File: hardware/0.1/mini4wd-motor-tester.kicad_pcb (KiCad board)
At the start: 2 copper layers, 93 parts, among them J1 USB_C_Receptacle_USB2.0_16P, J2 JST SH, J3 JST SH, M1 Motor_DC, SW1 RA, SW2 RA, SW3 EC11, U1 TLV62130, U2 USBLC6-2SC6, U3 RT9080-33GJ5, U4 MCP4725, U5 ESP32-S3-WROOM-1, U6 INA219AxDCN, U7 DRV8837, U8 GP2S700HCP, U9 TMP1075DSG

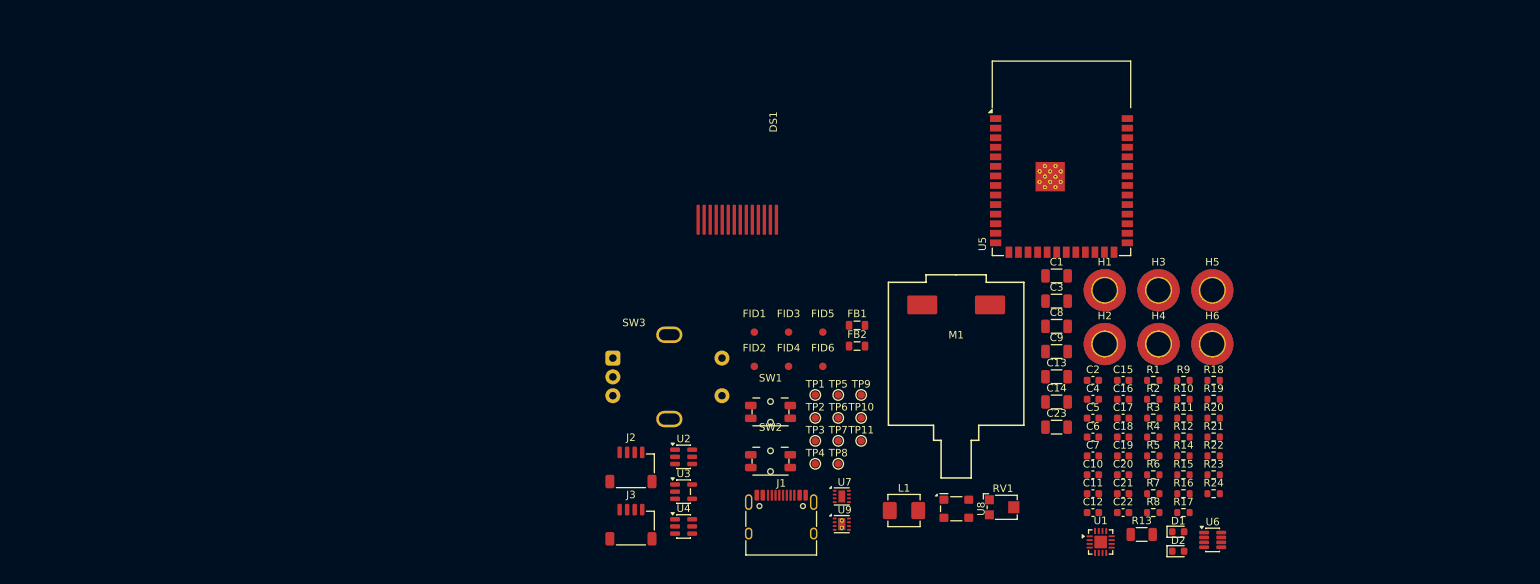
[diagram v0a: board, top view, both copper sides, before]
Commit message: rough component placement
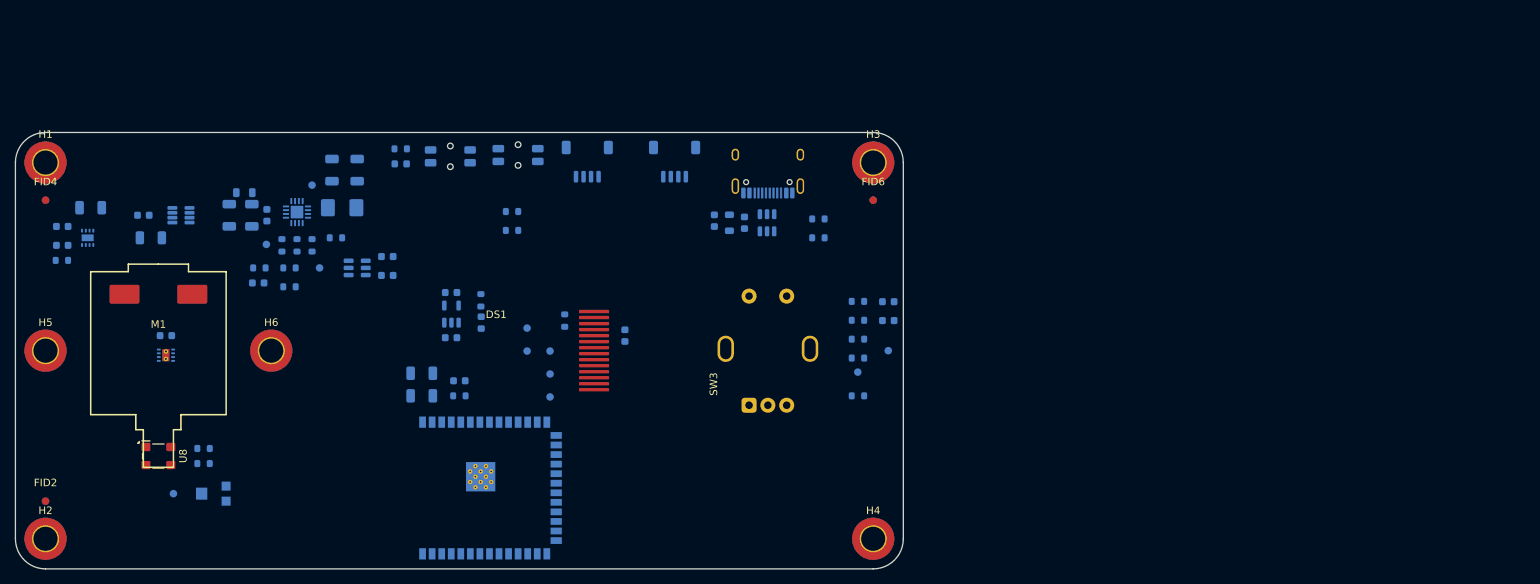
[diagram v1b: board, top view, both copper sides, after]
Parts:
- C1, C10, C11, C12, C13, C14, C15, C16, C17, C18, C19, C2, C20, C21, C22, C23, C3, C4, C5, C6, C7, C8, C9, D1, D2, FB1, FB2, FID1, FID3, FID5, J1, J2, J3, L1, R1, R10, R11, R12, R13, R14, R15, R16, R17, R18, R19, R2, R20, R21, R22, R23, R24, R3, R4, R5, R6, R7, R8, R9, RV1, SW1, SW2, TP1, TP10, TP11, TP2, TP3, TP4, TP5, TP6, TP7, TP8, TP9, U1, U2, U3, U4, U5, U6, U7, U9: moved to B.Cu
- moved H5 155.3 mm to (70.0, 100.0)
- moved R11 150.5 mm to (72.2, 88.0), turned to 180 degrees
- moved U6 143.7 mm to (88.0, 82.0), turned to 180 degrees
- moved C17 143.3 mm to (72.2, 83.5)
- moved H2 143.1 mm to (70.0, 125.0)
- moved C16 142.5 mm to (72.2, 86.0)
- moved H1 141.8 mm to (70.0, 75.0)
- moved R13 137.5 mm to (84.0, 85.0), turned to 180 degrees
- moved R22 134.2 mm to (91.0, 113.0), turned to 180 degrees
- moved C15 132.0 mm to (83.0, 82.0), turned to 180 degrees
- moved C23 131.6 mm to (76.0, 81.0)
- moved R17 130.4 mm to (91.0, 115.0), turned to 180 degrees
- moved C22 129.4 mm to (86.0, 98.0), turned to 180 degrees
- moved H6 125.1 mm to (100.0, 100.0)
- moved R9 121.1 mm to (101.4, 86.0), turned to -90 degrees
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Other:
- board outline added: 118 x 58 mm

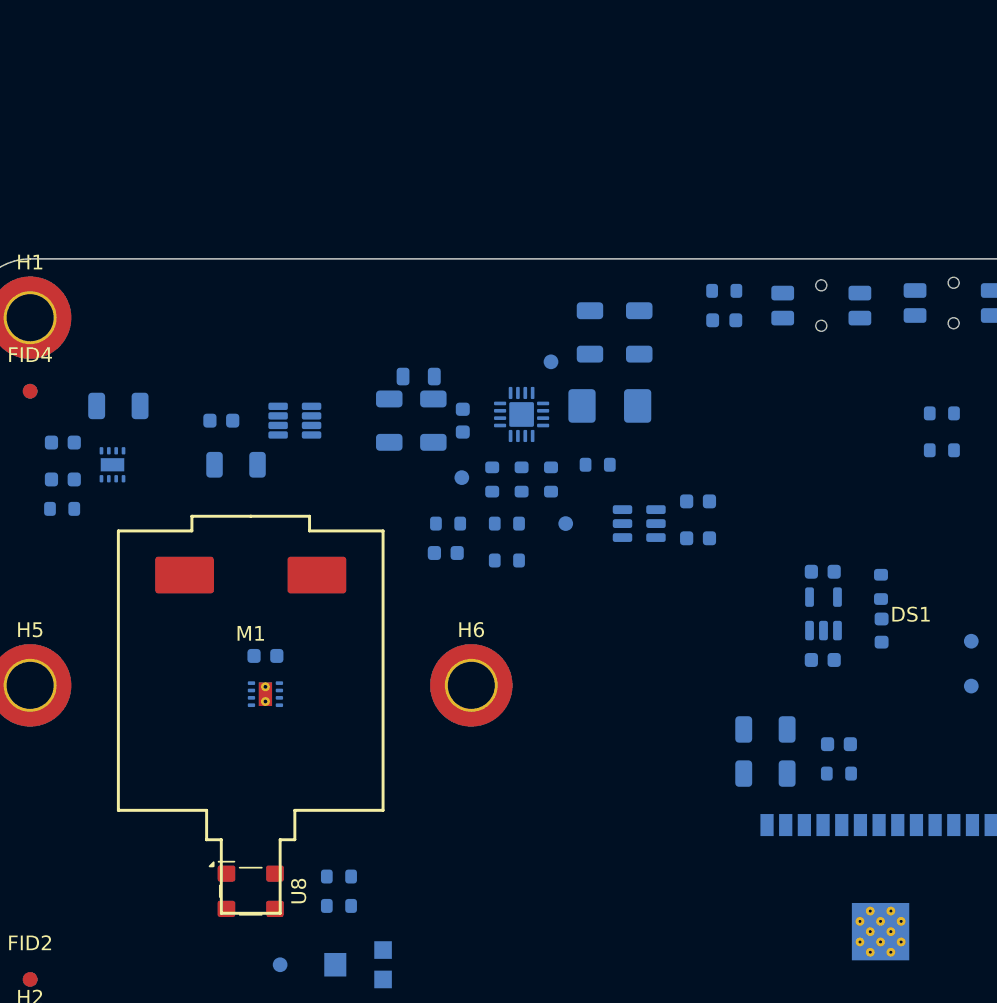
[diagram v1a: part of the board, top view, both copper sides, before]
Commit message: add wheel rpm, aux 5V circuits
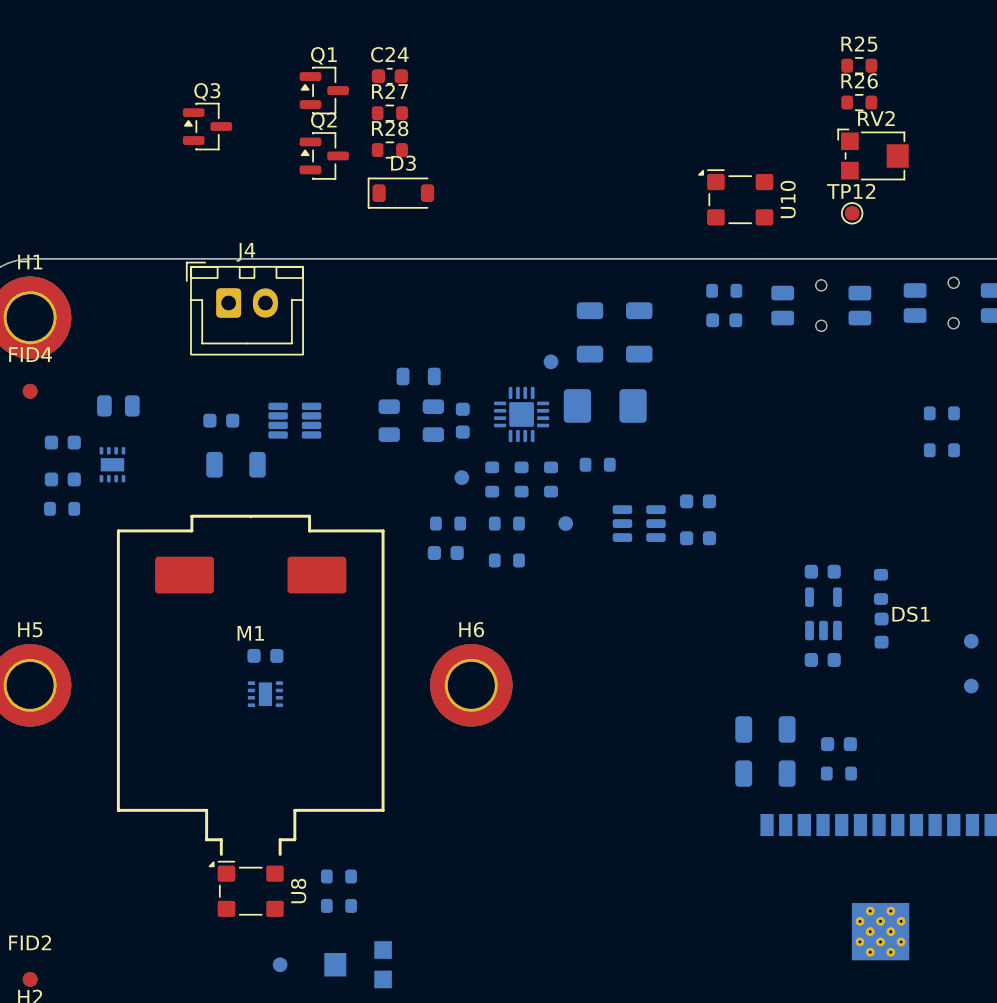
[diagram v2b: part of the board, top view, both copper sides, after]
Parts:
- added C24: 100n, Capacitor_SMD:C_0603_1608Metric, F.Cu at (94.5, 58.6)
- added D3: B5819W, Diode_SMD:D_SOD-123, F.Cu at (95.4, 66.5)
- added J4: JST XH, Connector_JST:JST_XH_B2B-XH-A_1x02_P2.50mm_Vertical, F.Cu at (83.5, 74.0)
- added Q1: 2N7002, Package_TO_SOT_SMD:SOT-23, F.Cu at (90.0, 59.5)
- added Q2: AO3401A, Package_TO_SOT_SMD:SOT-23, F.Cu at (90.0, 64.0)
- added Q3: 2N7002, Package_TO_SOT_SMD:SOT-23, F.Cu at (82.1, 62.0)
- added R25: 22R, Resistor_SMD:R_0603_1608Metric, F.Cu at (126.4, 57.9)
- added R26: 2K2, Resistor_SMD:R_0603_1608Metric, F.Cu at (126.4, 60.4)
- added R27: 10K, Resistor_SMD:R_0603_1608Metric, F.Cu at (94.5, 61.1)
- added R28: 10K, Resistor_SMD:R_0603_1608Metric, F.Cu at (94.5, 63.6)
- added RV2: POT_10K, josh-passives-smt:Potentiometer_Bourns_TC33X_Vertical, F.Cu at (127.5, 64.0)
- added TP12: TP, TestPoint:TestPoint_Pad_D1.0mm, F.Cu at (125.9, 67.9)
- added U10: GP2S700HCP, josh-passives-smt:Sharp_GP2S700HCP, F.Cu at (118.3, 67.0)
- C1, C23, C3: footprint Capacitor_SMD:C_1206_3216Metric -> Capacitor_SMD:C_0805_2012Metric
- U9: footprint Package_SON:WSON-8-1EP_2x2mm_P0.5mm_EP0.9x1.6mm_ThermalVias -> Package_SON:WSON-8-1EP_2x2mm_P0.5mm_EP0.9x1.6mm
- moved L1 0.31 mm to (109.1, 81.0)
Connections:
- net /RPM_OUT renamed /MOTOR_OUT
- U5 pad 38: unconnected-(U5-IO2-Pad38) -> /AUX_5V_EN
- U5 pad 39: unconnected-(U5-IO1-Pad39) -> /WHEEL_OUT

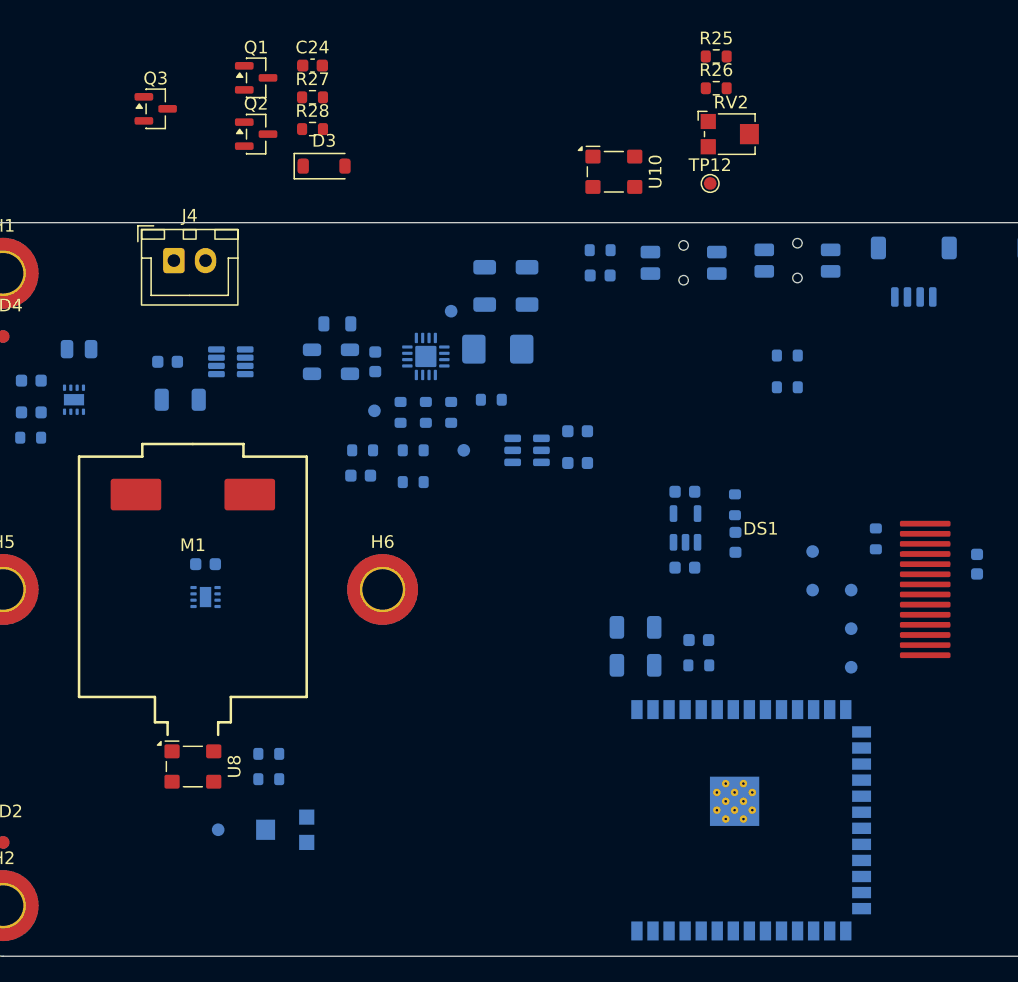
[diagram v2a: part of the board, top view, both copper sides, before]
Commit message: update motor cutout, provision space for wheel speed tester
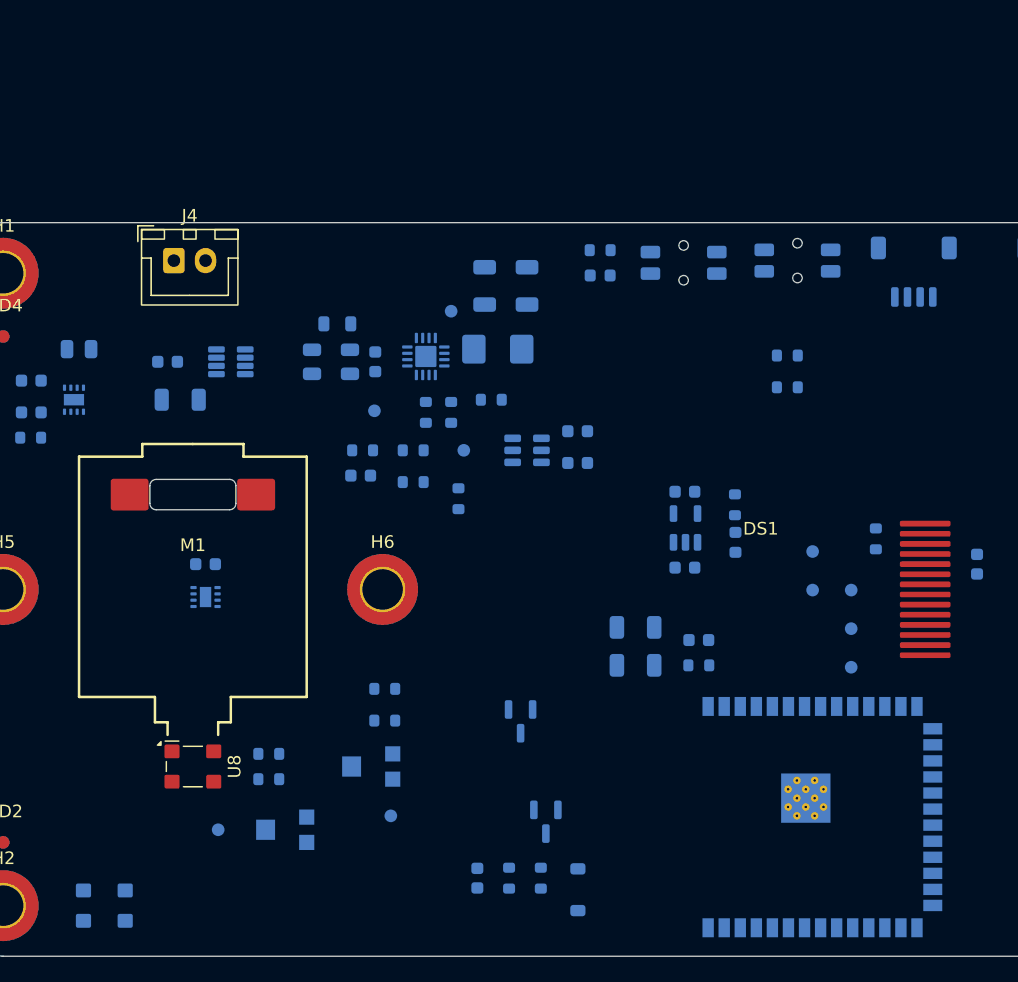
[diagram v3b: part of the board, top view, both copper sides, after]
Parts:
- removed Q1: 2N7002, Package_TO_SOT_SMD:SOT-23
- C24, D3, Q2, Q3, R25, R26, R27, R28, RV2, TP12, U10: moved to B.Cu
- R8: value 22K -> 30K
- R9: value 75K -> 100K
- moved U10 70.6 mm to (78.0, 125.0), turned to 180 degrees
- moved C24 65.6 mm to (107.5, 122.8), turned to -90 degrees
- moved R27 63.7 mm to (110.0, 122.8), turned to -90 degrees
- moved R28 61.9 mm to (112.5, 122.8), turned to -90 degrees
- moved D3 60.6 mm to (115.4, 123.7), turned to -90 degrees
- moved Q2 59.0 mm to (112.9, 118.4), turned to -90 degrees
- moved RV2 57.6 mm to (99.0, 114.0), turned to 180 degrees
- moved R25 56.5 mm to (100.2, 107.9), turned to 180 degrees
- moved R26 56.5 mm to (100.2, 110.4), turned to 180 degrees
- moved Q3 56.4 mm to (110.9, 110.4), turned to -90 degrees
- moved TP12 56.0 mm to (100.7, 117.9), turned to 180 degrees
- moved R9 8.22 mm to (106.0, 92.8), turned to 90 degrees
- moved U5 5.64 mm to (131.0, 118.0)

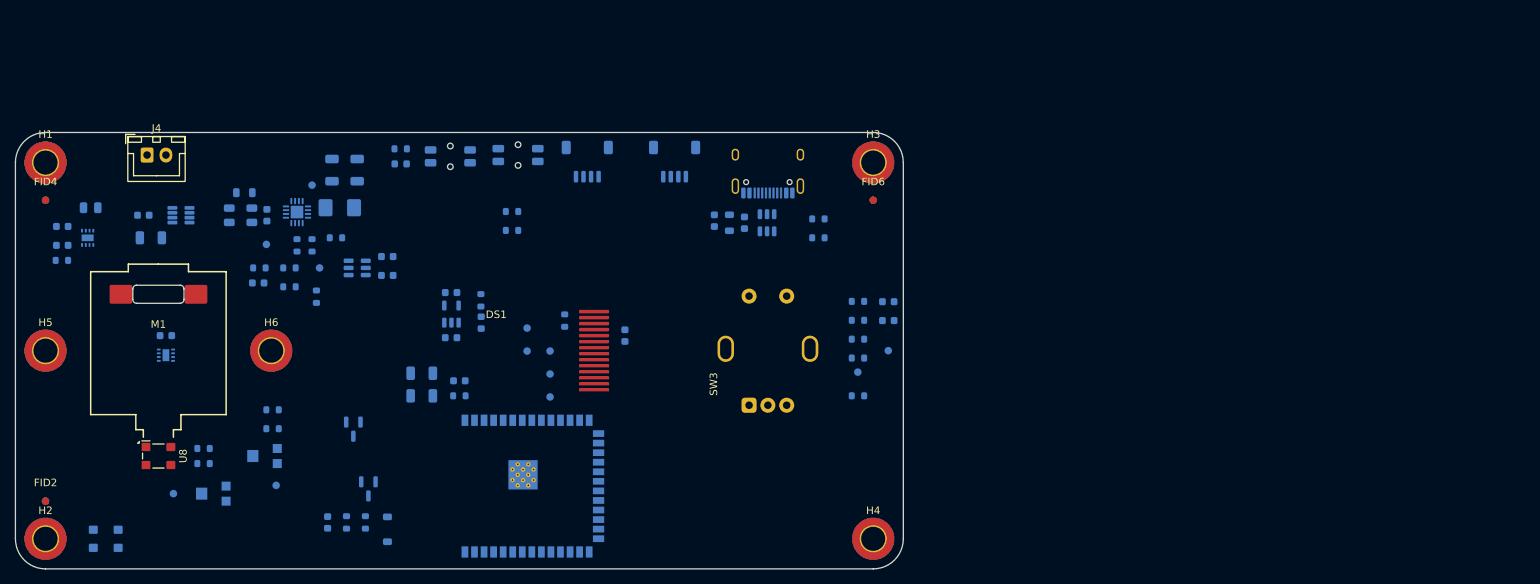
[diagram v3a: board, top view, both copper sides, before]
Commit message: shrinking board down
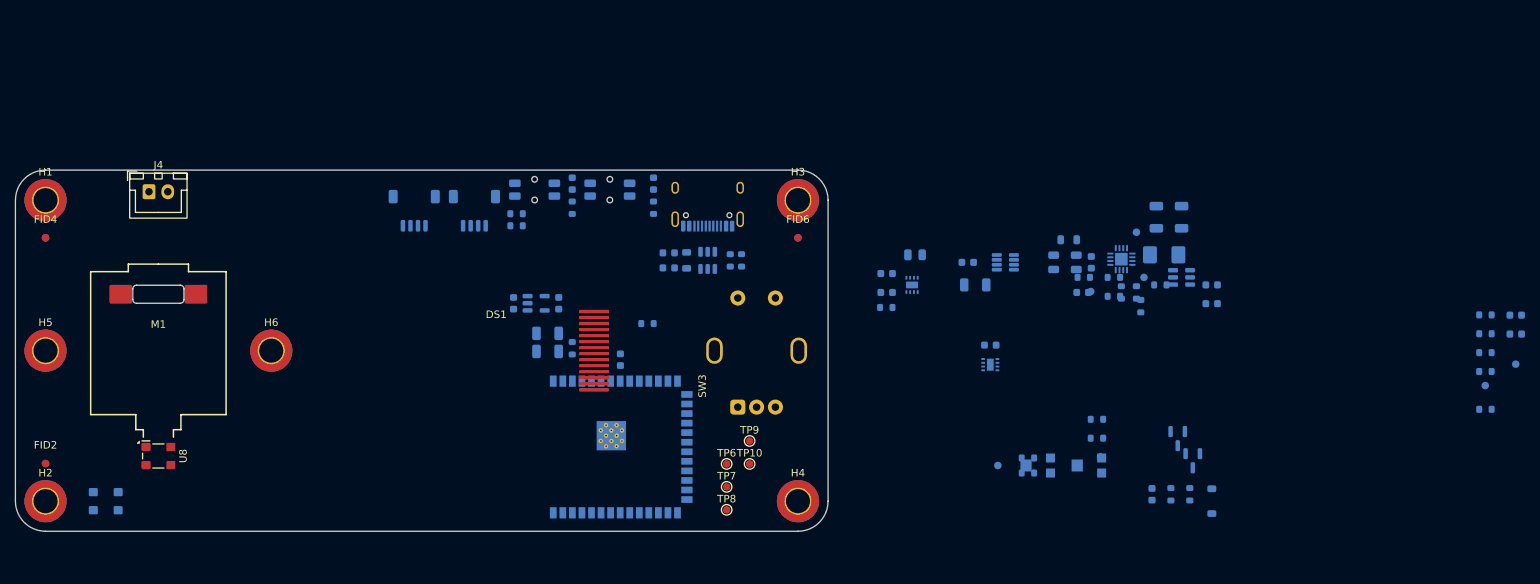
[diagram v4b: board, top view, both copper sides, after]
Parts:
- removed C18: 1u, Capacitor_SMD:C_0603_1608Metric
- TP10, TP6, TP7, TP8, TP9: moved to F.Cu
- moved L1 109.7 mm to (218.7, 87.3)
- moved R11 109.7 mm to (181.7, 94.3)
- moved C15 109.7 mm to (192.6, 88.3)
- moved C16 109.7 mm to (181.8, 92.3)
- moved C17 109.7 mm to (181.8, 89.8)
- moved C23 109.7 mm to (185.6, 87.3)
- moved C9 109.7 mm to (217.6, 82.3)
- moved R13 109.7 mm to (193.6, 91.3)
- moved R6 109.7 mm to (218.2, 91.3)
- moved U6 109.7 mm to (197.6, 88.3)
- moved U7 109.7 mm to (185.2, 91.3)
- moved C1 109.7 mm to (204.0, 88.3)
- moved C12 109.7 mm to (225.0, 93.8)
- moved C3 109.7 mm to (207.0, 88.3)
- moved C4 109.7 mm to (209.0, 88.3)
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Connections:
- net Net-(J2-Pin_3) renamed /TXD
- net Net-(J2-Pin_4) renamed /RXD
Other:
- board size 118 x 58 mm -> 108 x 48 mm
